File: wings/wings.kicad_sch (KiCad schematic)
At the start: 9 parts, among them U1 VBPW34S, U2 VBPW34S, U3 VBPW34S, U4 VBPW34S

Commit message: big panel, new wing
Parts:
- removed U1, U2, U3, U4: VBPW34S, VBPW34S:SENSOR-SMD_L4.4-W3.9, symbol VBPW34S:VBPW34S
- added B1, B2: KXOB25-03X4F-TB, KXOB25-03X4F:KXOB25_AAR, symbol KXOB25-03X4F:KXOB25-03X4F-TB

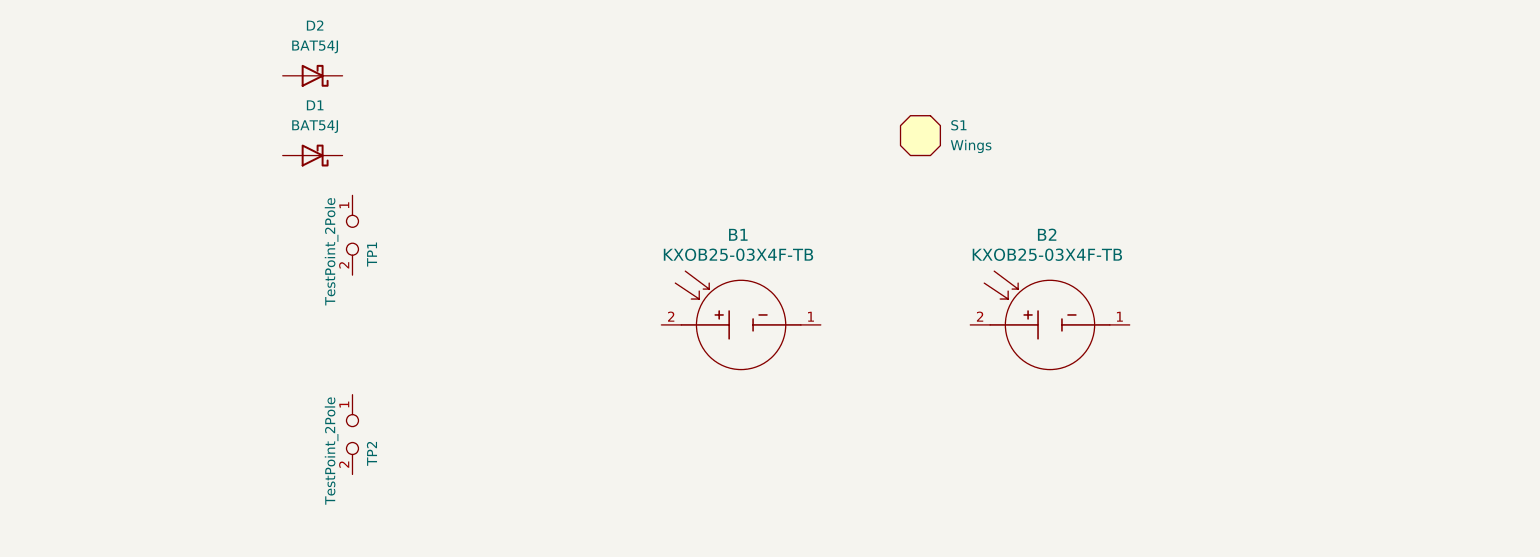
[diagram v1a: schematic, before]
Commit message: tracks for wings
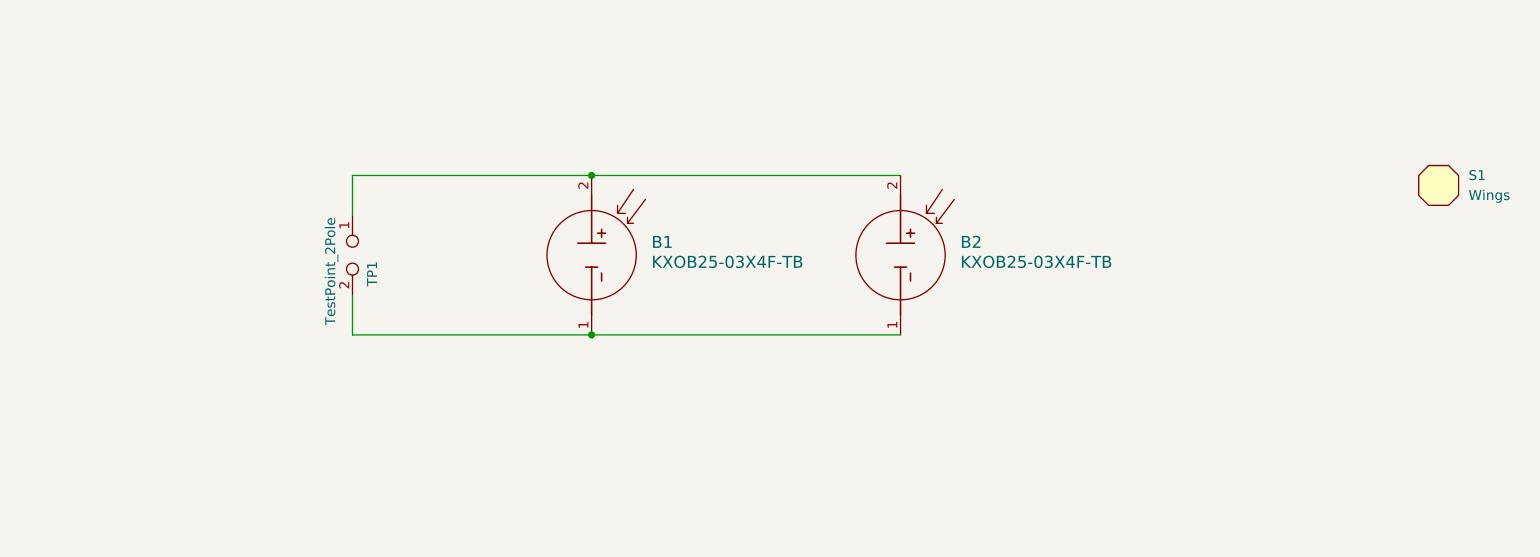
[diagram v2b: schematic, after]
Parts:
- removed D1, D2: BAT54J, Diode_SMD:D_SOD-323F, symbol Diode:BAT54J
- removed TP2: TestPoint_2Pole, Connector_PinSocket_2.54mm:PinSocket_2x01_P2.54mm_Vertical, symbol Connector:TestPoint_2Pole
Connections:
- net at B1.1: now also B2.1, TP1.2
- net at B1.2: now also B2.2, TP1.1
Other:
- moved on the sheet: B1, B2, S1, TP1
